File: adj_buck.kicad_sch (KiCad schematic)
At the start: 18 parts, among them U5 TPS54540BDDA, U6 MCP41100T-I/SN

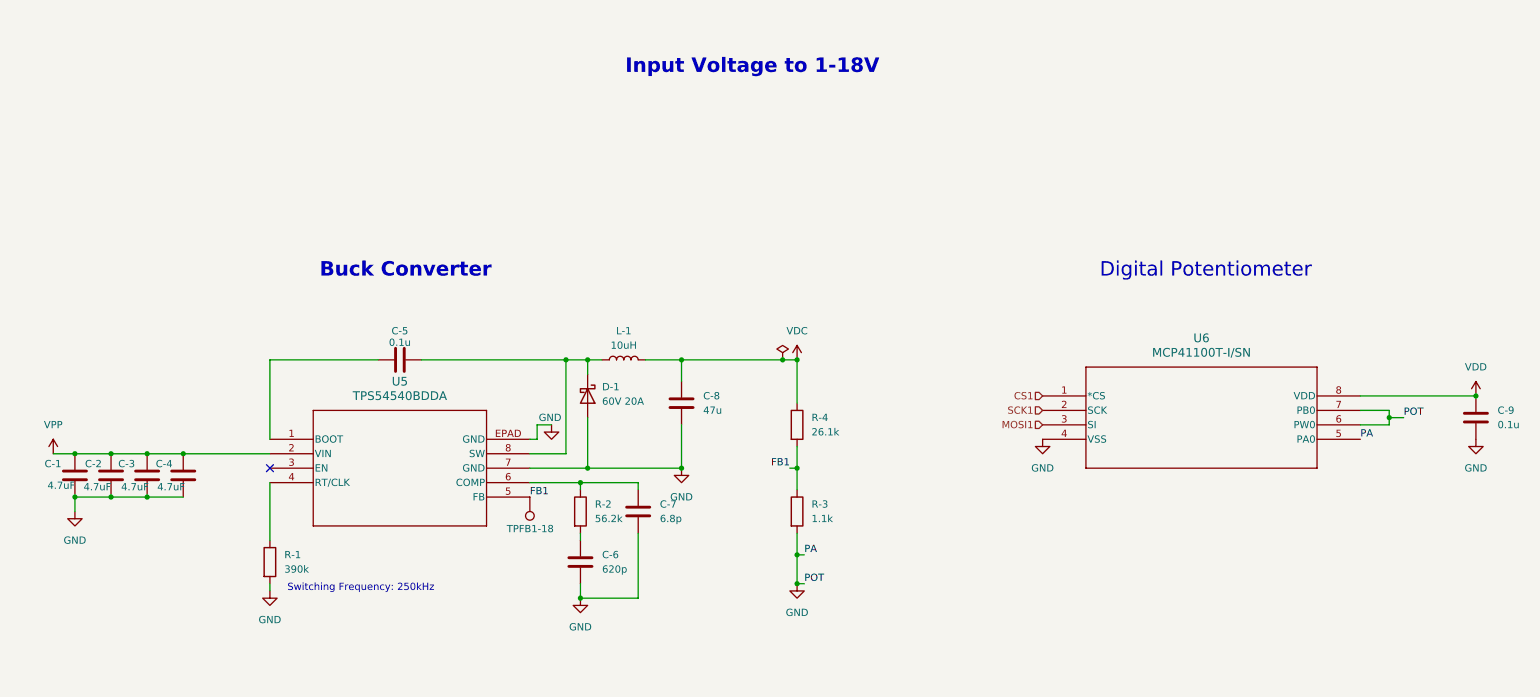
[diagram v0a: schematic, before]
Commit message: Rename references, update symbols and schematic layout
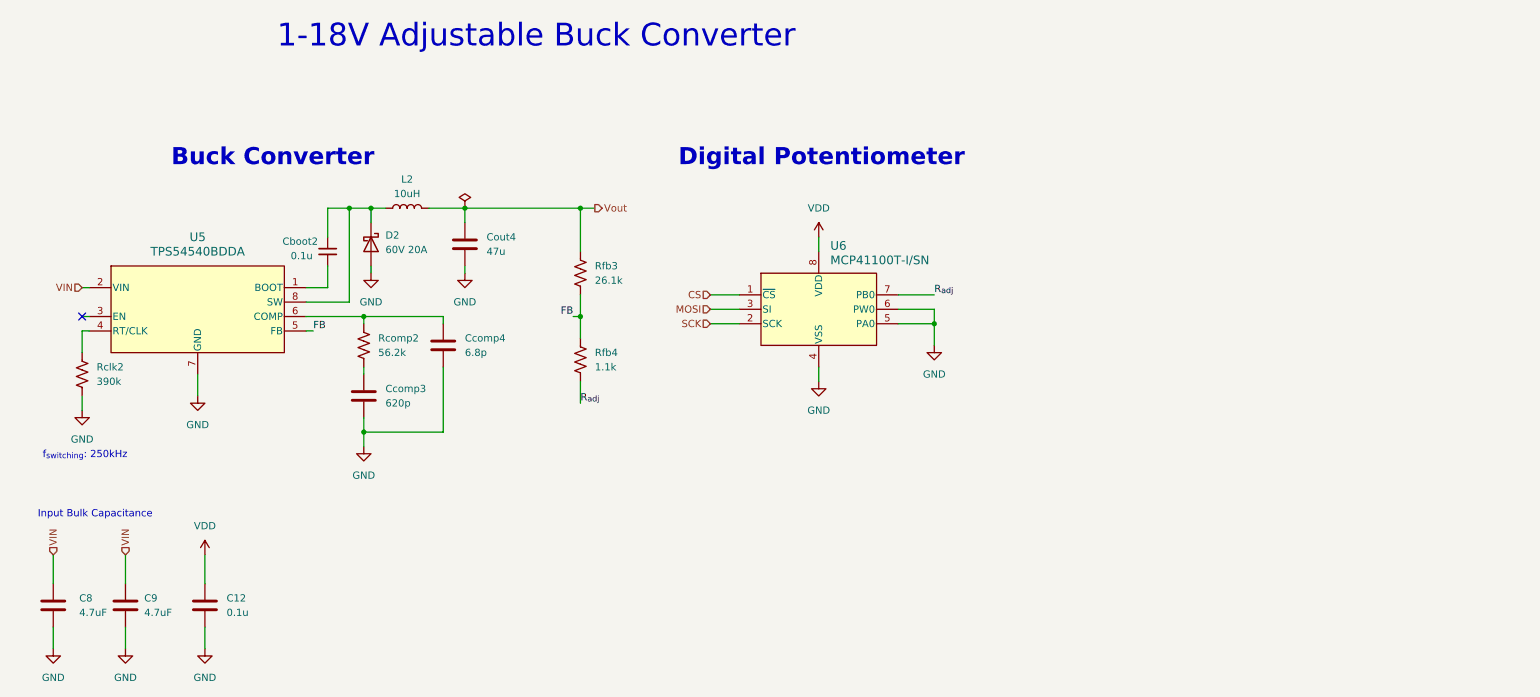
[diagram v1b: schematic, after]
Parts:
- removed C-1, C-2, C-3, C-4: 4.7uF, Capacitor_SMD:C_0805_2012Metric, symbol Device:C
- removed C-5, C-9: 0.1u, Capacitor_SMD:C_0805_2012Metric, symbol Device:C
- removed TPFB1-18: TestPoint, TestPoint:TestPoint_Loop_D2.60mm_Drill0.9mm_Beaded, symbol Connector:TestPoint
- added C12: 0.1u, Capacitor_SMD:C_0805_2012Metric, symbol Device:C
- added C8, C9: 4.7uF, Capacitor_SMD:C_0805_2012Metric, symbol Device:C
- added Cboot2: 0.1u, Capacitor_SMD:C_0805_2012Metric, symbol Device:C_Small
- Rclk2: renamed from R-1; symbol Device:R -> Device:R_US
- Rcomp2: renamed from R-2; symbol Device:R -> Device:R_US
- Rfb3: renamed from R-4; symbol Device:R -> Device:R_US
- Rfb4: renamed from R-3; symbol Device:R -> Device:R_US
- U5: symbol 2026-07-22_15-59-22:TPS54540BDDA -> LEOS:TPS54540BDDA
- U6: footprint LEOS:SOIC8-N_MC_MCH -> Package_SO:SOIC-8_3.9x4.9mm_P1.27mm; symbol 2026-10-07_18-01-27:MCP41100T-I_SN -> LEOS:MCP41100T-I_SN
- renumbered C-6 to Ccomp3, C-7 to Ccomp4, C-8 to Cout4, D-1 to D2, L-1 to L2
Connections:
- net GND: now also C12.2, C8.2, C9.2; no longer Rfb4.2, U6.7 (PB0)
- net VDD: now also C12.1
- net at D2.1 (K), L2.1, U5.8 (SW): now also Cboot2.1
- net at U5.1 (BOOT): now also Cboot2.2
- net CS1 renamed CS
- net FB1 renamed FB
- net MOSI1 renamed MOSI
- net SCK1 renamed SCK
- net VDC renamed Vout
- net VPP renamed VIN
- net VIN: now also C8.1, C9.1
- new net R_{adj}: Rfb4.2, U6.7 (PB0)
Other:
- note added: "1-18V Adjustable Buck Converter"
- note added: "Input Bulk Capacitance"
- note added: "f_{switching}: 250kHz"
- note removed: "Input Voltage to 1-18V"
- note removed: "Switching Frequency: 250kHz"
- company: (none) -> VIP Lightning From the Edge of Space
- moved on the sheet: Ccomp3, Ccomp4, Cout4, D2, L2
